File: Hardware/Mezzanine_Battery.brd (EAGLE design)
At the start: 30.5 x 44.5 mm, 10 parts, among them U2 EDISON_CONNECTOR_FULLMOUNTING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, U3 EDISON_CONNECTOR_FULLHEADER

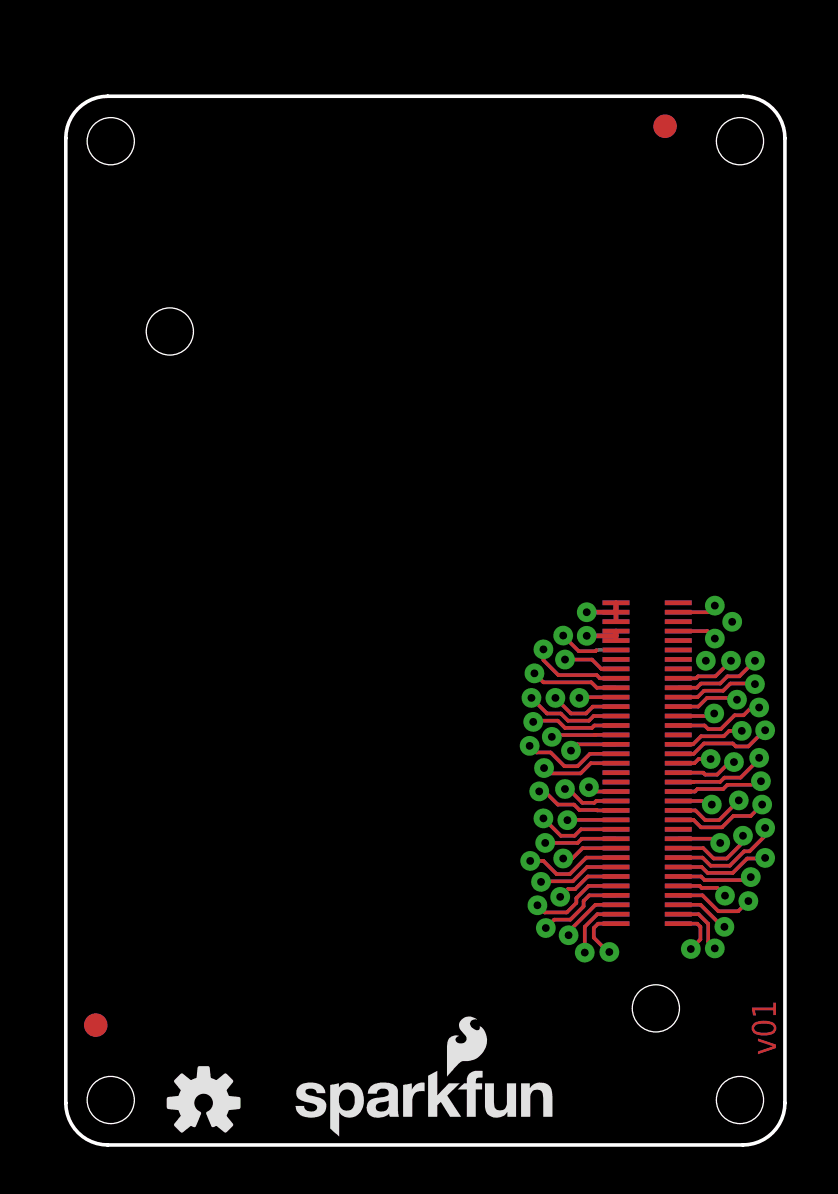
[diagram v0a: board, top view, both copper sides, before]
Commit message: layout ready for review. Renamed boards
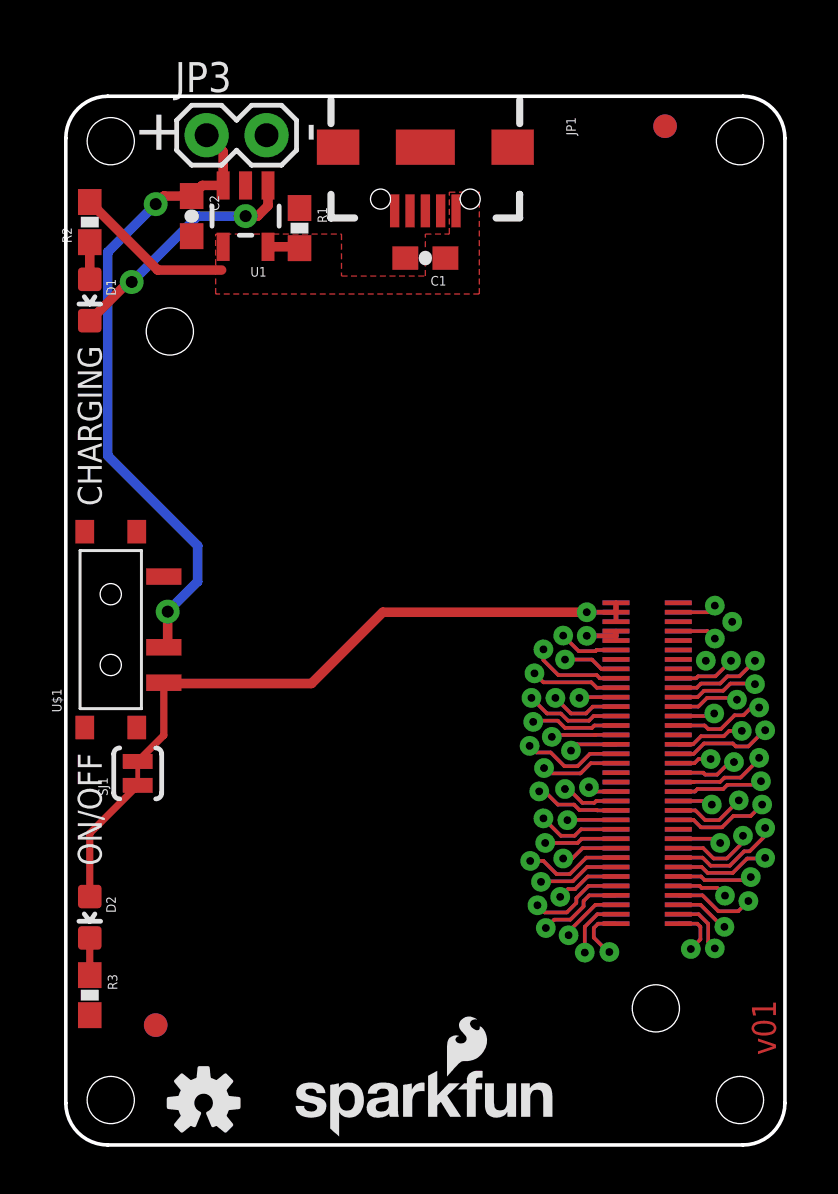
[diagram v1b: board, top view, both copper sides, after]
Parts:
- added C1, C2: 4.7uF, SparkFun-Capacitors:0603-CAP
- added D1: RED, SparkFun-LED:LED-0603
- added D2: BLUE, SparkFun-LED:LED-0603
- added FID3, FID4: FIDUCIAL1X2, SparkFun-Aesthetics:FIDUCIAL-1X2
- added JP1: USB_MICROB_PLUGCONN-11752, SparkFun-Connectors:USB-B-MICRO-SMD_V03
- added JP3: M02PTH, SparkFun-Connectors:1X02
- added R1: 2.0k, SparkFun-Resistors:0603-RES
- added R2: 330, SparkFun-Resistors:0603-RES
- added R3: 1k, SparkFun-Resistors:0603-RES
- added SJ1: JUMPER-PAD-2-NC_BY_TRACE, SparkFun-Passives:PAD-JUMPER-2-NC_BY_TRACE_YES_SILK
- added U$1: SWITCH_SPDT, SparkFun-Electromechanical:KPS-1290
- added U1: MCP73831, SparkFun-PowerIC:SOT23-5
- moved FID1 2.54 mm to (3.81, 5.08)
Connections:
- new net N$1: C1.1, JP1.VBUS1, R2.2, U1.4
- new net N$2: D2.C, R3.1
- new net N$3: R1.2, U1.5
- new net N$4: D1.A, R2.1
- new net N$5: D1.C, U1.1
- new net N$6: C2.1, JP3.1, U$1.P, U1.3
- new net N$7: D2.A, SJ1.1
- net GND: now also C1.2, C2.2, JP1.GND1, JP1.SHIELD1, JP1.SHIELD2, JP1.SHIELD3, JP3.2, R1.1, R3.2, U1.2
- net VSYS: now also SJ1.2, U$1.S
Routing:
- net N$6: track 0.00 -> 27.4 mm, vias 0 -> 2
- net VSYS: track 4.48 -> 27.5 mm
- net N$5: track 0.00 -> 10.6 mm, vias 0 -> 2
- net N$1: track 0.00 -> 6.78 mm
- net N$7: track 0.00 -> 5.55 mm
- net N$2: track 0.00 -> 1.58 mm
- net N$4: track 0.00 -> 1.57 mm
- net N$3: track 0.00 -> 1.36 mm
- net 1.8V: track 4.25 -> 5.07 mm
- added copper zone on layer 1, net N$1
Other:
- board text added: "+"
- board text added: "-"
- board text added: "CHARGING"
- board text added: "Edzzanine Battery"
- board text added: "OFF/ON"
- board text added: "ON/OFF"
- board text removed: "Example Name of Board"
